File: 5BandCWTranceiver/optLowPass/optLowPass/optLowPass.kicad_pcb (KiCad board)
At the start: 2 copper layers, 60.2 x 113 mm, 74 parts, among them J1 Conn_01x06_Male, J2 Conn_01x02_Male, J3 Conn_Coaxial, J4 Conn_Coaxial, J5 Conn_01x02_Male, J6 Conn_01x02_Male, J7 Conn_01x02_Male, J8 Conn_01x02_Male, K1 G5V-2, K2 G5V-2, K3 G5V-2, K4 G5V-2, K5 G5V-2, Q1 MMBT3904, Q2 MMBT3904, Q3 MMBT3904, Q4 MMBT3904, Q5 MMBT3904

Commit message: First Tapeout
First tapeout of AptLowPass to JLCPCB
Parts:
- added C32: 628p, Capacitor_THT:C_Disc_D4.3mm_W1.9mm_P5.00mm, F.Cu at (114.3, 64.2)
- added C33: 89p, Capacitor_THT:C_Disc_D4.3mm_W1.9mm_P5.00mm, F.Cu at (135.3, 57.2)
- added C34: 1218p, Capacitor_THT:C_Disc_D4.3mm_W1.9mm_P5.00mm, B.Cu at (127.1, 54.5)
- added C35: 202p, Capacitor_THT:C_Disc_D4.3mm_W1.9mm_P5.00mm, F.Cu at (135.3, 46.5)
- added C36: 557p, Capacitor_THT:C_Disc_D4.3mm_W1.9mm_P5.00mm, B.Cu at (127.1, 45.2)
- added C37: 435p, Capacitor_THT:C_Disc_D4.3mm_W1.9mm_P5.00mm, F.Cu at (114.1, 87.2)
- added C38: 62p, Capacitor_THT:C_Disc_D4.3mm_W1.9mm_P5.00mm, F.Cu at (135.3, 78.8)
- added C39: 844p, Capacitor_THT:C_Disc_D4.3mm_W1.9mm_P5.00mm, B.Cu at (127.1, 76.8)
- added C40: 140p, Capacitor_THT:C_Disc_D4.3mm_W1.9mm_P5.00mm, F.Cu at (135.3, 68.2)
- added C41: 386p, Capacitor_THT:C_Disc_D4.3mm_W1.9mm_P5.00mm, B.Cu at (127.1, 67.8)
- added C42: 314p, Capacitor_THT:C_Disc_D4.3mm_W1.9mm_P5.00mm, F.Cu at (114.3, 107.5)
- added C43: 44p, Capacitor_THT:C_Disc_D4.3mm_W1.9mm_P5.00mm, F.Cu at (135.6, 100.0)
- added C44: 609p, Capacitor_THT:C_Disc_D4.3mm_W1.9mm_P5.00mm, B.Cu at (127.3, 97.5)
- added C45: 101p, Capacitor_THT:C_Disc_D4.3mm_W1.9mm_P5.00mm, F.Cu at (135.6, 89.5)
- added C46: 279p, Capacitor_THT:C_Disc_D4.3mm_W1.9mm_P5.00mm, B.Cu at (127.1, 89.5)
- added C47: 244p, Capacitor_THT:C_Disc_D4.3mm_W1.9mm_P5.00mm, F.Cu at (114.3, 128.5)
- added C48: 35p, Capacitor_THT:C_Disc_D4.3mm_W1.9mm_P5.00mm, F.Cu at (135.6, 121.0)
- added C49: 474p, Capacitor_THT:C_Disc_D4.3mm_W1.9mm_P5.00mm, B.Cu at (127.1, 119.0)
- added C50: 79p, Capacitor_THT:C_Disc_D4.3mm_W1.9mm_P5.00mm, F.Cu at (135.6, 110.5)
- added C51: 217p, Capacitor_THT:C_Disc_D4.3mm_W1.9mm_P5.00mm, B.Cu at (127.3, 109.5)
- added C52: 209p, Capacitor_THT:C_Disc_D4.3mm_W1.9mm_P5.00mm, F.Cu at (113.8, 149.5)
- added C53: 30p, Capacitor_THT:C_Disc_D4.3mm_W1.9mm_P5.00mm, F.Cu at (135.6, 142.2)
- added C54: 406p, Capacitor_THT:C_Disc_D4.3mm_W1.9mm_P5.00mm, B.Cu at (127.3, 140.0)
- added C55: 67p, Capacitor_THT:C_Disc_D4.3mm_W1.9mm_P5.00mm, F.Cu at (135.3, 131.8)
- added C56: 186p, Capacitor_THT:C_Disc_D4.3mm_W1.9mm_P5.00mm, B.Cu at (127.3, 131.2)
- C10, C11, C12, C13, C14, C15, C16, C17, C18, C22, C23, C24, C25, C26, C27, C28, C29, C30, C31, C4, C5, C6, C7, C8, C9: footprint Library:C_Disc_DUAL_D4.3mm_W1.9mm_P5.00mm -> Capacitor_THT:C_Disc_D4.3mm_W1.9mm_P5.00mm
- moved J3 5.33 mm to (103.1, 150.5)
- moved C22 1.66 mm to (114.3, 125.8)
- moved C4 1.31 mm to (114.3, 61.7)
- moved C6 1.18 mm to (114.3, 104.8)
- moved C5 0.80 mm to (114.1, 84.5)
- moved J4 0.10 mm to (103.6, 42.5)
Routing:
- net Net-(J3-In): track 0.00 -> 257.7 mm, vias 0 -> 1
- net (no net): track 192.6 -> 0.00 mm
- net Net-(J4-In): track 0.00 -> 145.6 mm
- net Net-(C17-Pad2): track 0.00 -> 37.0 mm
- net Net-(C22-Pad1): track 0.00 -> 36.7 mm
- net Net-(C18-Pad2): track 0.00 -> 36.5 mm
- net Net-(C16-Pad2): track 0.00 -> 35.8 mm
- net Net-(C10-Pad1): track 0.00 -> 34.7 mm
- net Net-(C26-Pad1): track 0.00 -> 34.3 mm
- net Net-(C11-Pad1): track 0.00 -> 34.2 mm
- net Net-(C12-Pad1): track 0.00 -> 33.8 mm
- net Net-(C27-Pad1): track 0.00 -> 33.6 mm
- net Net-(C23-Pad1): track 3.87 -> 36.5 mm
- net Net-(C25-Pad1): track 0.00 -> 25.1 mm
- net Net-(C10-Pad2): track 0.00 -> 24.9 mm
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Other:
- board text added: "N7WMN OptLowPass LPF Board Rev. A"
- board text removed: "N7WM OptLowPass LPF Board Rev. A"
- board text removed: "to transmitter"

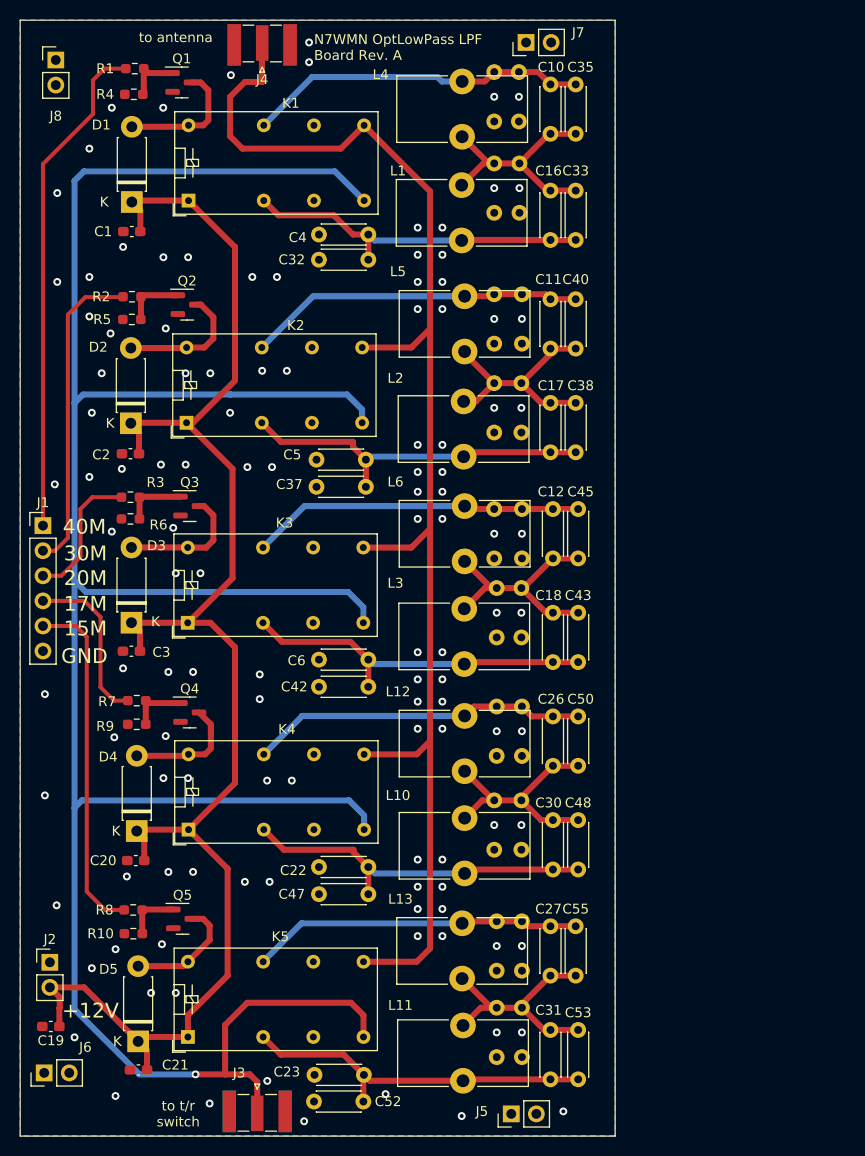
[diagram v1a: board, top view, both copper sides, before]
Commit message: Ready for tapeout
Filter board now with diode switching and SMD caps; power amp board updated with beefier dual nmos.
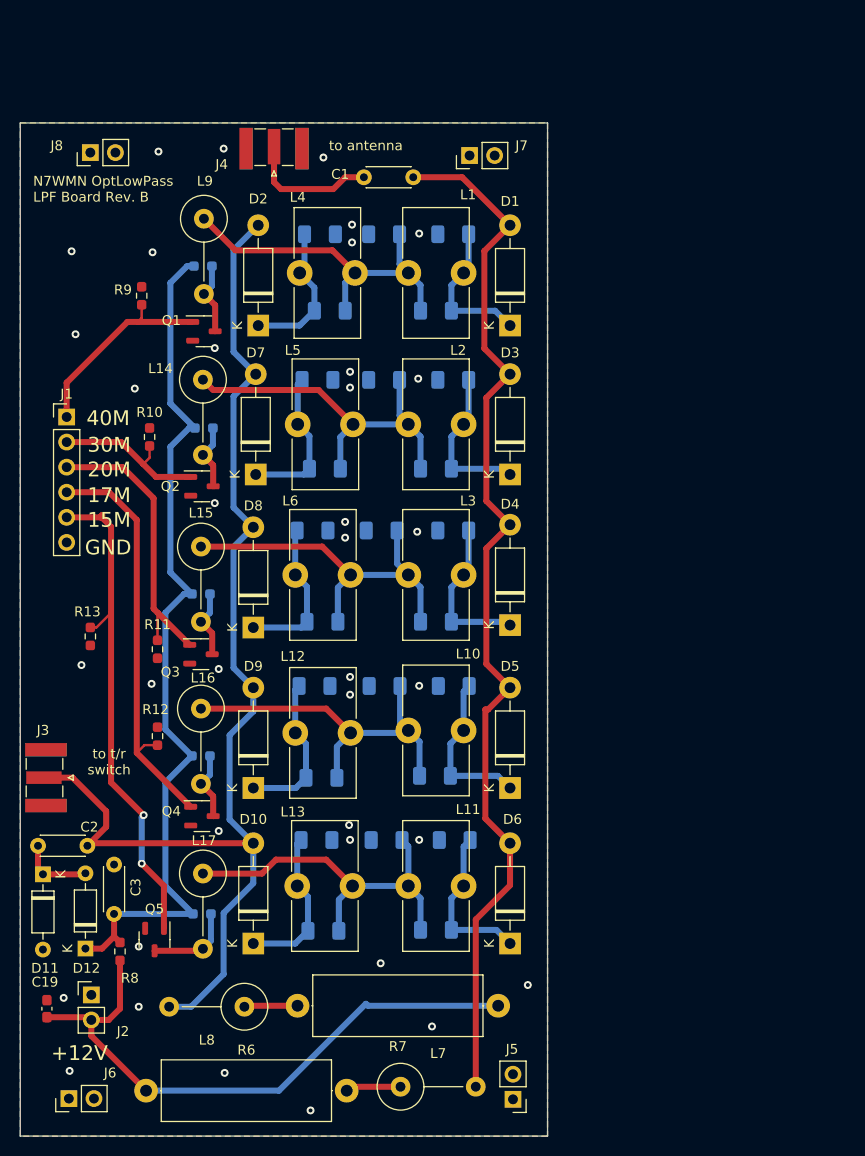
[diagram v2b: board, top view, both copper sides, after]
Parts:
- removed C11: 140p, Capacitor_THT:C_Disc_D4.3mm_W1.9mm_P5.00mm
- removed C14: 386p, Capacitor_THT:C_Disc_D4.3mm_W1.9mm_P5.00mm
- removed C16: 89p, Capacitor_THT:C_Disc_D4.3mm_W1.9mm_P5.00mm
- removed C17: 62p, Capacitor_THT:C_Disc_D4.3mm_W1.9mm_P5.00mm
- removed C20, C21: 0.1uF, Capacitor_SMD:C_0603_1608Metric_Pad1.08x0.95mm_HandSolder
- removed C22: 244p, Capacitor_THT:C_Disc_D4.3mm_W1.9mm_P5.00mm
- removed C24: 474p, Capacitor_THT:C_Disc_D4.3mm_W1.9mm_P5.00mm
- removed C25: 406p, Capacitor_THT:C_Disc_D4.3mm_W1.9mm_P5.00mm
- removed C26: 79p, Capacitor_THT:C_Disc_D4.3mm_W1.9mm_P5.00mm
- removed C29: 186p, Capacitor_THT:C_Disc_D4.3mm_W1.9mm_P5.00mm
- removed C30: 35p, Capacitor_THT:C_Disc_D4.3mm_W1.9mm_P5.00mm
- removed C31: 30p, Capacitor_THT:C_Disc_D4.3mm_W1.9mm_P5.00mm
- removed C35: 202p, Capacitor_THT:C_Disc_D4.3mm_W1.9mm_P5.00mm
- removed C36: 557p, Capacitor_THT:C_Disc_D4.3mm_W1.9mm_P5.00mm
- removed C4: 628p, Capacitor_THT:C_Disc_D4.3mm_W1.9mm_P5.00mm
- removed C42: 314p, Capacitor_THT:C_Disc_D4.3mm_W1.9mm_P5.00mm
- removed C43: 44p, Capacitor_THT:C_Disc_D4.3mm_W1.9mm_P5.00mm
- removed C45: 101p, Capacitor_THT:C_Disc_D4.3mm_W1.9mm_P5.00mm
- removed C46: 279p, Capacitor_THT:C_Disc_D4.3mm_W1.9mm_P5.00mm
- removed C5: 435p, Capacitor_THT:C_Disc_D4.3mm_W1.9mm_P5.00mm
- removed C51: 217p, Capacitor_THT:C_Disc_D4.3mm_W1.9mm_P5.00mm
- removed C52: 209p, Capacitor_THT:C_Disc_D4.3mm_W1.9mm_P5.00mm
- removed C55: 67p, Capacitor_THT:C_Disc_D4.3mm_W1.9mm_P5.00mm
- removed C7: 1218p, Capacitor_THT:C_Disc_D4.3mm_W1.9mm_P5.00mm
- removed C8: 844p, Capacitor_THT:C_Disc_D4.3mm_W1.9mm_P5.00mm
- removed C9: 609p, Capacitor_THT:C_Disc_D4.3mm_W1.9mm_P5.00mm
- removed K1, K2, K3, K4, K5: G5V-2, Relay_THT:Relay_DPDT_Omron_G5V-2
- added D10: 1N4007, Diode_THT:D_DO-41_SOD81_P10.16mm_Horizontal, F.Cu at (102.7, 133.5)
- added D11: 1N914, Diode_THT:D_DO-35_SOD27_P7.62mm_Horizontal, F.Cu at (81.4, 126.5)
- added D12: 1N914, Diode_THT:D_DO-35_SOD27_P7.62mm_Horizontal, F.Cu at (85.7, 134.0)
- added D6: 1N4007, Diode_THT:D_DO-41_SOD81_P10.16mm_Horizontal, F.Cu at (128.7, 133.5)
- added D7: 1N4007, Diode_THT:D_DO-41_SOD81_P10.16mm_Horizontal, F.Cu at (103.0, 86.0)
- added D8: 1N4007, Diode_THT:D_DO-41_SOD81_P10.16mm_Horizontal, F.Cu at (102.7, 101.5)
- added D9: 1N4007, Diode_THT:D_DO-41_SOD81_P10.16mm_Horizontal, F.Cu at (102.7, 117.8)
- added L14: 47uH, Inductor_THT:L_Axial_L11.0mm_D4.5mm_P7.62mm_Vertical_Fastron_MECC, F.Cu at (97.6, 76.4)
- added L15: 47uH, Inductor_THT:L_Axial_L11.0mm_D4.5mm_P7.62mm_Vertical_Fastron_MECC, F.Cu at (97.4, 93.3)
- added L16: 47uH, Inductor_THT:L_Axial_L11.0mm_D4.5mm_P7.62mm_Vertical_Fastron_MECC, F.Cu at (97.4, 109.7)
- added L17: 47uH, Inductor_THT:L_Axial_L11.0mm_D4.5mm_P7.62mm_Vertical_Fastron_MECC, F.Cu at (97.6, 126.4)
- added L7: 47uH, Inductor_THT:L_Axial_L11.0mm_D4.5mm_P7.62mm_Vertical_Fastron_MECC, F.Cu at (117.6, 148.0)
- added L8: 47uH, Inductor_THT:L_Axial_L11.0mm_D4.5mm_P7.62mm_Vertical_Fastron_MECC, F.Cu at (101.8, 139.9)
- added L9: 47uH, Inductor_THT:L_Axial_L11.0mm_D4.5mm_P7.62mm_Vertical_Fastron_MECC, F.Cu at (97.7, 60.1)
- added R11: 47K, Resistor_SMD:R_0603_1608Metric_Pad0.98x0.95mm_HandSolder, F.Cu at (93.0, 103.7)
- added R12: 47K, Resistor_SMD:R_0603_1608Metric_Pad0.98x0.95mm_HandSolder, F.Cu at (93.0, 112.5)
- added R13: 47K, Resistor_SMD:R_0603_1608Metric_Pad0.98x0.95mm_HandSolder, F.Cu at (86.2, 102.4)
- C1: footprint Capacitor_SMD:C_0603_1608Metric_Pad1.08x0.95mm_HandSolder -> Capacitor_THT:C_Disc_D4.3mm_W1.9mm_P5.00mm
- C10, C12, C18, C23, C27, C32, C33, C37, C38, C40, C47, C48, C50, C53, C6: footprint Capacitor_THT:C_Disc_D4.3mm_W1.9mm_P5.00mm -> Capacitor_SMD:C_1206_3216Metric_Pad1.33x1.80mm_HandSolder; moved to B.Cu
- C13, C15, C28, C34, C39, C41, C44, C49, C54, C56: footprint Capacitor_THT:C_Disc_D4.3mm_W1.9mm_P5.00mm -> Capacitor_SMD:C_1206_3216Metric_Pad1.33x1.80mm_HandSolder
- C2: value 0.1uF -> 15pF; footprint Capacitor_SMD:C_0603_1608Metric_Pad1.08x0.95mm_HandSolder -> Capacitor_THT:C_Disc_D4.3mm_W1.9mm_P5.00mm
- C3: value 0.1uF -> 470pF; footprint Capacitor_SMD:C_0603_1608Metric_Pad1.08x0.95mm_HandSolder -> Capacitor_THT:C_Disc_D4.3mm_W1.9mm_P5.00mm
- D1, D2, D3, D4, D5: value 1N4152 -> 1N4007; footprint Diode_THT:D_DO-41_SOD81_P7.62mm_Horizontal -> Diode_THT:D_DO-41_SOD81_P10.16mm_Horizontal
- Q1, Q2, Q3, Q4, Q5: value MMBT3904 -> BSS123; footprint Package_TO_SOT_SMD:SOT-23 -> Package_TO_SOT_SMD:SOT-23-3
- R1, R2, R3: value 2K -> 47K; moved to B.Cu
- R10, R9: value 3K -> 47K
- R4, R5: value 3K -> 47K; moved to B.Cu
- R6: value 3K -> 560; footprint Resistor_SMD:R_0603_1608Metric_Pad0.98x0.95mm_HandSolder -> Resistor_THT:R_Axial_DIN0617_L17.0mm_D6.0mm_P20.32mm_Horizontal
- R7: value 2K -> 560; footprint Resistor_SMD:R_0603_1608Metric_Pad0.98x0.95mm_HandSolder -> Resistor_THT:R_Axial_DIN0617_L17.0mm_D6.0mm_P20.32mm_Horizontal
- R8: value 2K -> 100K
- moved R4 67.3 mm to (97.4, 114.5)
- moved R5 60.6 mm to (97.5, 130.5)
- moved R6 57.9 mm to (91.8, 148.4), turned to 0 degrees
- moved R10 50.3 mm to (92.2, 82.2), turned to -90 degrees
- moved R7 47.9 mm to (127.5, 139.8)
- moved D5 45.6 mm to (128.7, 117.8)
- moved R9 43.4 mm to (91.4, 67.9), turned to -90 degrees
- moved D4 43.2 mm to (128.7, 101.2)
- moved D3 41.2 mm to (128.7, 86.0)
- moved C2 40.8 mm to (80.9, 123.6), turned to 0 degrees
- moved D1 40.3 mm to (128.7, 70.9)
- moved J3 40.0 mm to (81.7, 116.7), turned to -90 degrees
- moved C10 32.0 mm to (110.5, 69.4), turned to 0 degrees
- moved C40 30.7 mm to (110.0, 85.4), turned to 0 degrees
- moved C50 26.7 mm to (109.6, 116.7), turned to 0 degrees
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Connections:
- C1 pad 1: /VDD12 -> Net-(J4-In)
- C1 pad 2: GND -> Net-(D1-A)
- C10 pad 1: Net-(C10-Pad1) -> Net-(D2-K)
- C13 pad 1: Net-(C10-Pad1) -> Net-(D2-K)
- C18 pad 2: Net-(C18-Pad2) -> Net-(D4-K)
- C19 pad 1: /VDD12 -> GND
- C19 pad 2: GND -> /VDD12
- C2 pad 1: /VDD12 -> Net-(D11-K)
- C2 pad 2: GND -> Net-(D10-A)
- C3 pad 1: /VDD12 -> /HV
- C32 pad 1: Net-(C16-Pad2) -> Net-(D1-K)
- C33 pad 2: Net-(C16-Pad2) -> Net-(D1-K)
- C37 pad 1: Net-(C17-Pad2) -> Net-(D3-K)
- C38 pad 2: Net-(C17-Pad2) -> Net-(D3-K)
- C47 pad 1: Net-(C22-Pad1) -> Net-(D5-K)
- C48 pad 2: Net-(C22-Pad1) -> Net-(D5-K)
- C6 pad 1: Net-(C18-Pad2) -> Net-(D4-K)
- D1 pad 1: /VDD12 -> Net-(D1-K)
- D2 pad 1: /VDD12 -> Net-(D2-K)
- D2 pad 2: Net-(D2-A) -> Net-(D10-A)
- D3 pad 1: /VDD12 -> Net-(D3-K)
- D3 pad 2: Net-(D3-A) -> Net-(D1-A)
- D4 pad 1: /VDD12 -> Net-(D4-K)
- D4 pad 2: Net-(D4-A) -> Net-(D1-A)
- D5 pad 1: /VDD12 -> Net-(D5-K)
- D5 pad 2: Net-(D5-A) -> Net-(D1-A)
- J1 pad 1: /40M -> Net-(J1-Pin_1)
- J1 pad 2: /30M -> Net-(J1-Pin_2)
- J1 pad 3: /20M -> Net-(J1-Pin_3)
- J1 pad 4: /17M -> Net-(J1-Pin_4)
- J1 pad 5: /15M -> Net-(J1-Pin_5)
- J3 pad 1: Net-(J3-In) -> Net-(D10-A)
- L1 pad 2: Net-(C16-Pad2) -> Net-(D1-K)
- L10 pad 2: Net-(C22-Pad1) -> Net-(D5-K)
- L2 pad 2: Net-(C17-Pad2) -> Net-(D3-K)
- L3 pad 2: Net-(C18-Pad2) -> Net-(D4-K)
- L4 pad 1: Net-(C10-Pad1) -> Net-(D2-K)
- Q1 pad 1: Net-(Q1-B) -> Net-(J1-Pin_1)
- Q1 pad 3: Net-(D1-A) -> Net-(Q1-D)
- Q2 pad 1: Net-(Q2-B) -> Net-(J1-Pin_2)
- Q2 pad 3: Net-(D2-A) -> Net-(Q2-D)
- Q3 pad 1: Net-(Q3-B) -> Net-(J1-Pin_3)
- Q3 pad 3: Net-(D3-A) -> Net-(Q3-D)
- Q4 pad 1: Net-(Q4-B) -> Net-(J1-Pin_4)
- Q4 pad 3: Net-(D4-A) -> Net-(Q4-D)
- Q5 pad 1: Net-(Q5-B) -> Net-(J1-Pin_5)
- Q5 pad 3: Net-(D5-A) -> Net-(Q5-D)
- R1 pad 1: Net-(Q1-B) -> Net-(Q1-D)
- R1 pad 2: /40M -> /HV
- R10 pad 1: Net-(Q5-B) -> GND
- R10 pad 2: GND -> Net-(J1-Pin_2)
- R2 pad 1: Net-(Q2-B) -> Net-(Q2-D)
- R2 pad 2: /30M -> /HV
- R3 pad 1: Net-(Q3-B) -> Net-(Q3-D)
- R3 pad 2: /20M -> /HV
- R4 pad 1: Net-(Q1-B) -> Net-(Q4-D)
- R4 pad 2: GND -> /HV
- R5 pad 1: Net-(Q2-B) -> Net-(Q5-D)
- R5 pad 2: GND -> /HV
- R6 pad 1: Net-(Q3-B) -> /VDD12
- R6 pad 2: GND -> Net-(L7-Pad1)
- R7 pad 1: Net-(Q4-B) -> /VDD12
- R7 pad 2: /17M -> Net-(L8-Pad1)
- R8 pad 1: Net-(Q5-B) -> /VDD12
- R8 pad 2: /15M -> /HV
- R9 pad 1: Net-(Q4-B) -> GND
- R9 pad 2: GND -> Net-(J1-Pin_1)
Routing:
- net Net-(J3-In): track 257.7 -> 0.00 mm, vias 1 -> 0
- net Net-(J4-In): track 145.6 -> 13.5 mm
- net Net-(D10-A): track 0.00 -> 120.6 mm
- net /VDD12: track 161.4 -> 61.7 mm
- net Net-(D1-A): track 13.1 -> 108.9 mm
- net /HV: track 0.00 -> 89.8 mm
- net Net-(J1-Pin_5): track 0.00 -> 51.0 mm, vias 0 -> 2
- net /40M: track 51.0 -> 0.00 mm
- net Net-(J1-Pin_4): track 0.00 -> 42.0 mm
- net Net-(C17-Pad2): track 37.0 -> 0.00 mm
- net Net-(C22-Pad1): track 36.7 -> 0.00 mm
- net Net-(C18-Pad2): track 36.5 -> 0.00 mm
- net Net-(C16-Pad2): track 35.8 -> 0.00 mm
- net /15M: track 35.2 -> 0.00 mm
- net Net-(C10-Pad1): track 34.7 -> 0.00 mm
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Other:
- board size 60.2 x 113 mm -> 53.4 x 102.6 mm
- board text added: "N7WMN OptLowPass LPF Board Rev. B"
- board text removed: "N7WMN OptLowPass LPF Board Rev. A"
